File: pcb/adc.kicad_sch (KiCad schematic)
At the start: 19 parts, among them U2 PCM1802DB, X1 ECS-2520MVLC-081.92

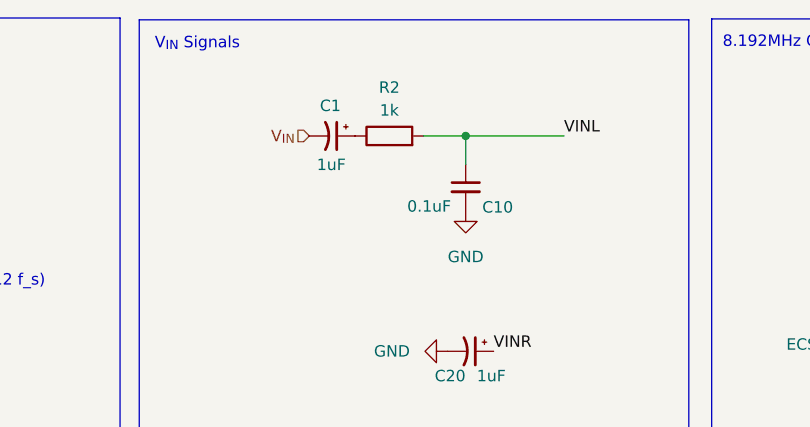
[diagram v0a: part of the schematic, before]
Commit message: Changed the LPF to 106 kHz cutoff
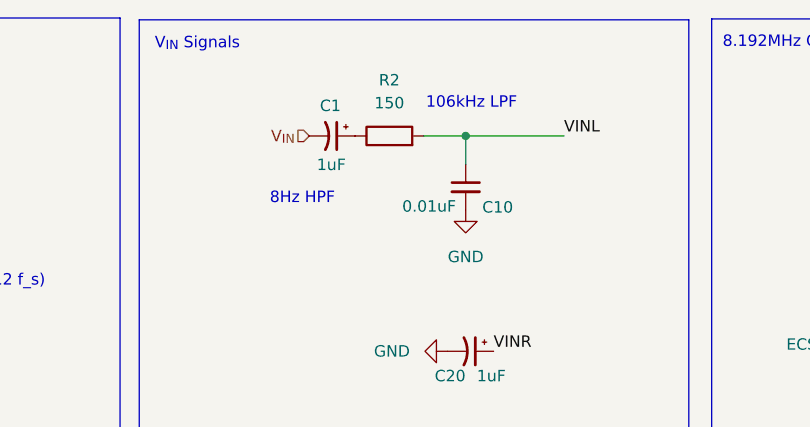
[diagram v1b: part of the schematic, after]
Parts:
- C10: value 0.1uF -> 0.01uF
- R2: value 1k -> 150
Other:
- note added: "106kHz LPF"
- note added: "8Hz HPF"
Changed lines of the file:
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@@
+    (effects (font (size 1.27 1.27)) (justify left bottom))
+  )
+  (text "8Hz HPF" (at 129.2352 73.6346 0)
     (effects (font (size 1.27 1.27)) (justify left bottom))
   )
   (text "Filter DC" (at 53.1114 114.8588 0)
+    (effects (font (size 1.27 1.27)) (justify left bottom))
+  )
+  (text "106kHz LPF" (at 146.5834 63.0428 0)
     (effects (font (size 1.27 1.27)) (justify left bottom))
   )
@@
   (symbol (lib_id "Device:R") (at 142.5194 65.8876 90) (unit 1)
     (in_bom yes) (on_board yes) (dnp no) (fields_autoplaced)
-    (property "Reference" "R2" (at 142.5194 60.5028 90)
-      (effects (font (size 1.27 1.27)))
-    )
-    (property "Value" "1k" (at 142.5194 63.0428 90)
+    (property "Reference" "R2" (at 142.5194 59.69 90)
+      (effects (font (size 1.27 1.27)))
+    )
+    (property "Value" "150" (at 142.5194 62.23 90)
       (effects (font (size 1.27 1.27)))
     )
@@
       (effects (font (size 1.27 1.27)))
     )
-    (property "Value" "0.1uF" (at 146.939 73.7108 0)
-      (effects (font (size 1.27 1.27)))
-    )
+    (property "Value" "0.01uF" (at 146.939 73.7108 0)
+      (effects (font (size 1.27 1.27)))
+    )

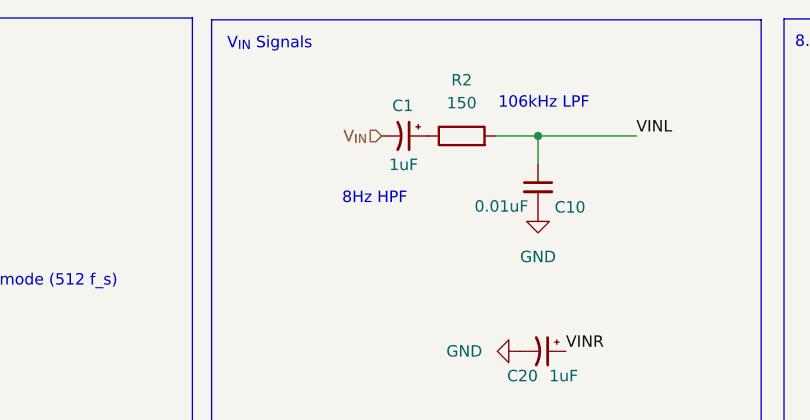
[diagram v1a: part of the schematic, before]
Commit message: Changed cap to nonpolarized to account for analog_in biasing scheme
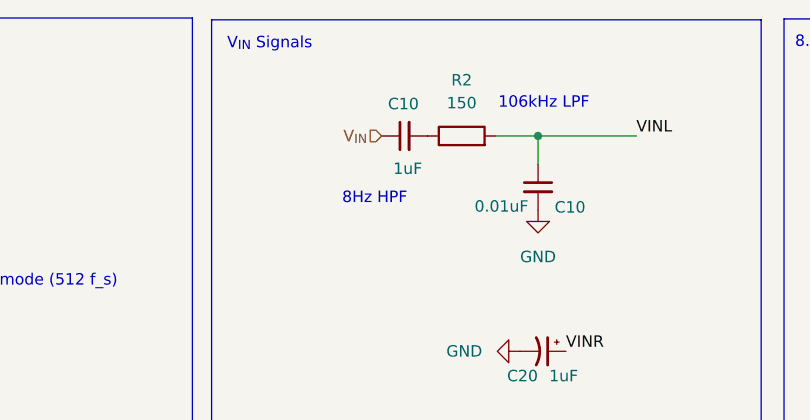
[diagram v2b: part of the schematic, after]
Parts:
- removed C1: 1uF, symbol Device:C_Polarized_Small_US
- added C10: 1uF, symbol Device:C_Small
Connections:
- net V_{IN}: now also C10.1
- net at R2.1: now also C10.2
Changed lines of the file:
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@@
-    )
-  )
-  (symbol (lib_id "Device:C_Polarized_Small_US") (at 136.1694 65.8876 270) (unit 1)
-    (in_bom yes) (on_board yes) (dnp no)
-    (property "Reference" "C1" (at 135.9662 62.5348 90)
-      (effects (font (size 1.27 1.27)))
-    )
-    (property "Value" "1uF" (at 136.0678 69.088 90)
-      (effects (font (size 1.27 1.27)))
-    )
-    (property "Footprint" "" (at 136.1694 65.8876 0)
-      (effects (font (size 1.27 1.27)) hide)
-    )
-    (property "Datasheet" "~" (at 136.1694 65.8876 0)
-      (effects (font (size 1.27 1.27)) hide)
-    )
-    (pin "1")
-    (pin "2")
-    (instances
-      (project "tuner_pedal"
-        (path "/be09f3cc-c79c-49de-93a4-4a01bf6bfbcf"
-          (reference "C1") (unit 1)
-        )
-        (path "/be09f3cc-c79c-49de-93a4-4a01bf6bfbcf/910ce163-1837-409b-9a8d-6a7a7eac3527"
-          (reference "C1") (unit 1)
-        )
-      )
     )
   )
@@
         )
       )
+    )
+  )
+  (symbol (lib_id "Device:C_Small") (at 136.1694 65.8876 90) (unit 1)
+    (in_bom yes) (on_board yes) (dnp no)
+    (property "Reference" "C10" (at 136.0424 62.3316 90)
+      (effects (font (size 1.27 1.27)))
+    )
+    (property "Value" "1uF" (at 136.525 69.5198 90)
+      (effects (font (size 1.27 1.27)))
+    )
+    (property "Footprint" "" (at 136.1694 65.8876 0)
+      (effects (font (size 1.27 1.27)) hide)
+    )
+    (property "Datasheet" "~" (at 136.1694 65.8876 0)
+      (effects (font (size 1.27 1.27)) hide)
+    )
+    (pin "1")
+    (pin "2")
+    (instances
+      (project "tuner_pedal"
+        (path "/be09f3cc-c79c-49de-93a4-4a01bf6bfbcf"
+          (reference "C10") (unit 1)
+        )
+        (path "/be09f3cc-c79c-49de-93a4-4a01bf6bfbcf/910ce163-1837-409b-9a8d-6a7a7eac3527"
+          (reference "C1") (unit 1)
+        )
+      )
